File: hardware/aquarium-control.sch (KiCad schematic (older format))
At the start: 27 parts, among them M1 CONN_1, M2 CONN_1, P1 Raspberry Pi, P2 Day, P3 Night, P4 Power, P5 Switch, U1 SN74HC04, U2 MDC3105D, U3 IM06GR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

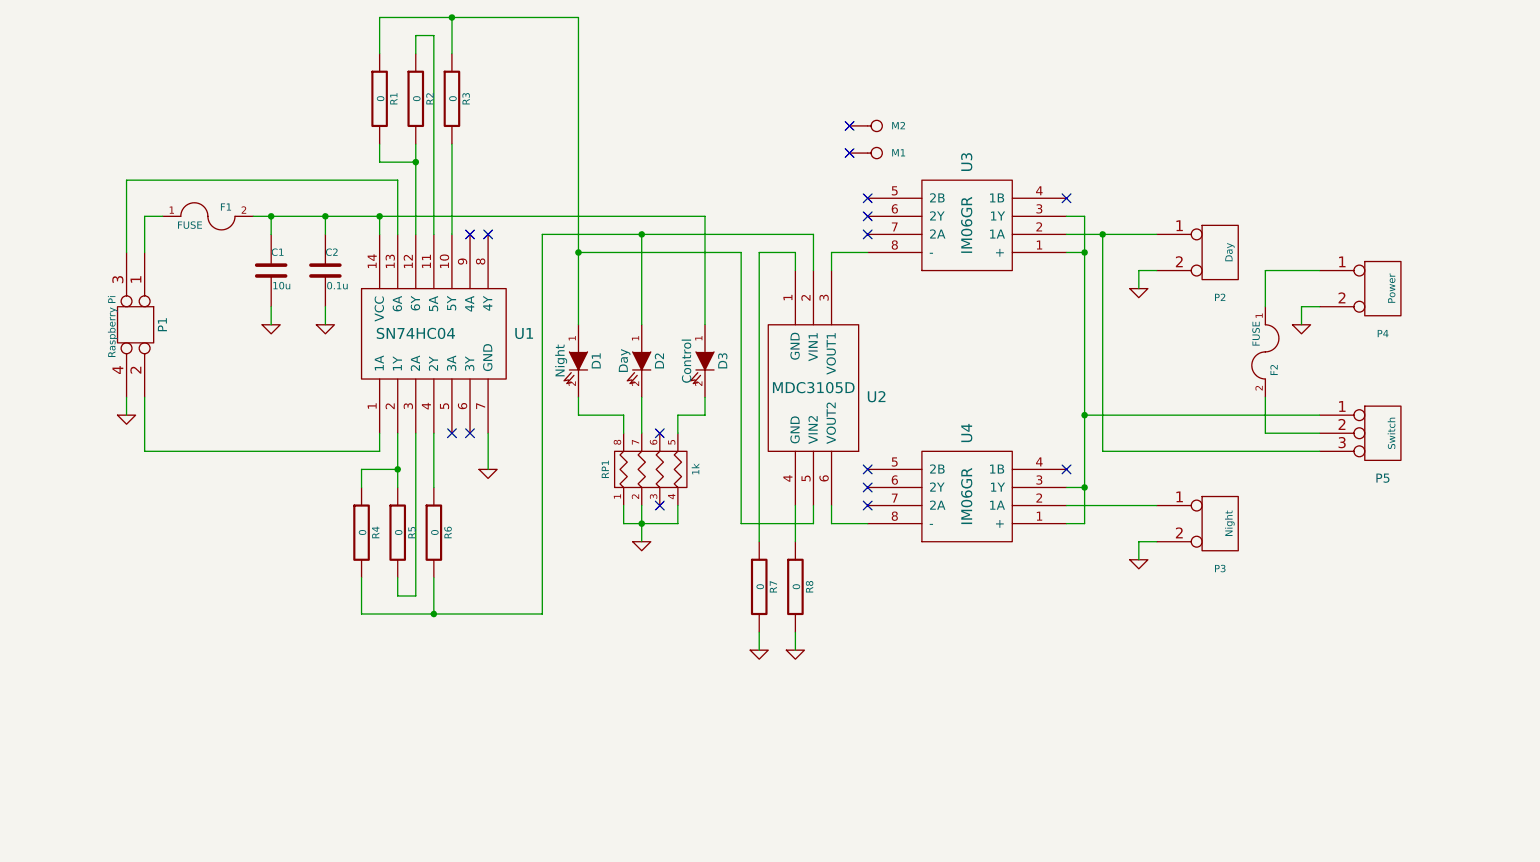
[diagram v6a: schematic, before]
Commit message: First draft of the v2 board
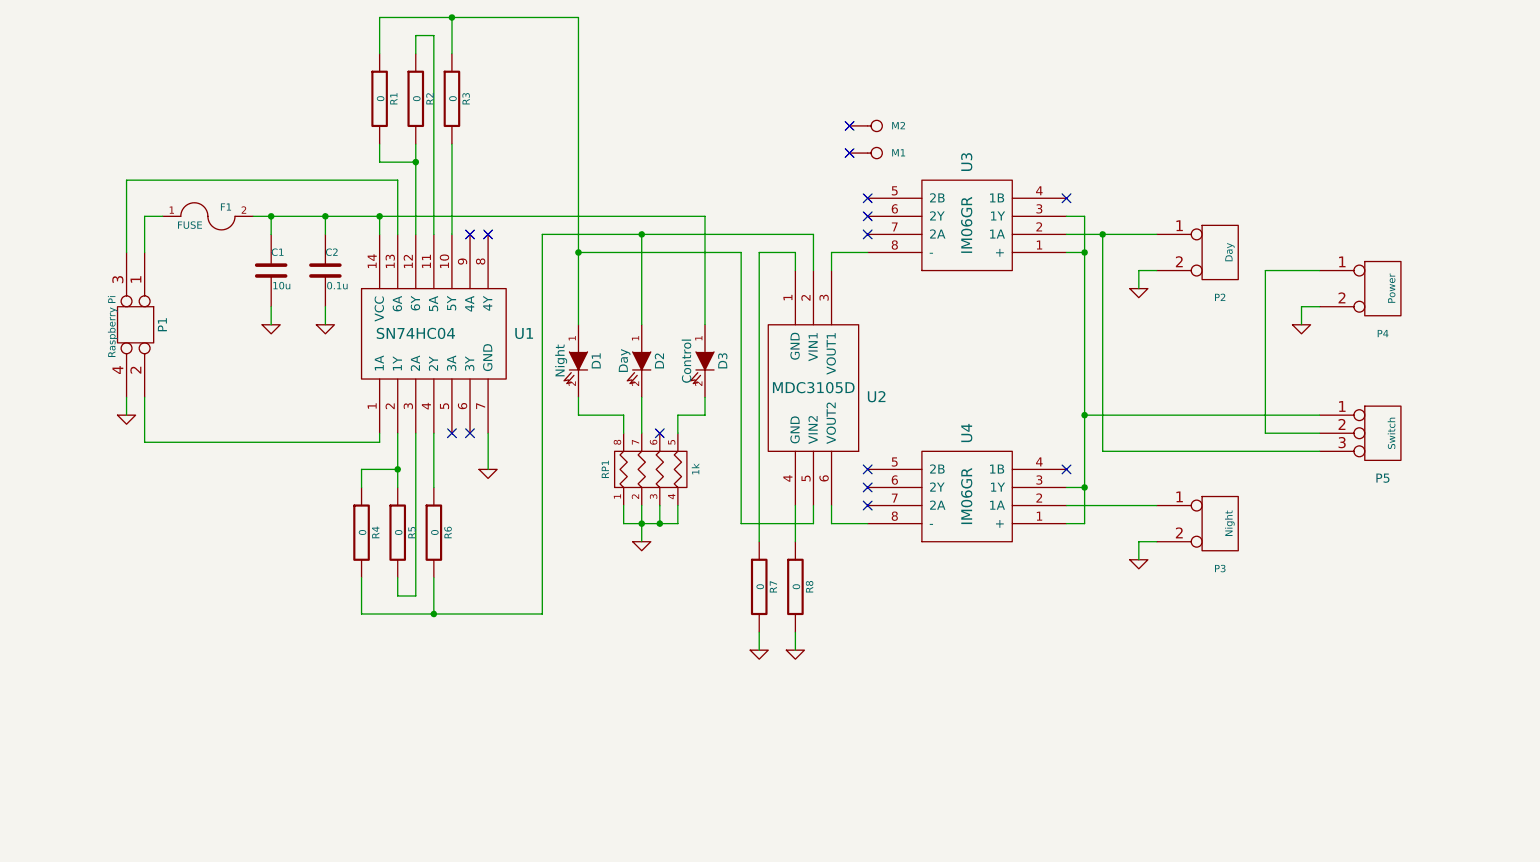
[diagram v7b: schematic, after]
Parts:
- removed F2: FUSE, symbol FUSE
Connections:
- net GND: now also RP1.3 (P3)
- net at P4.1 (P1): now also P5.2 (PM)
- no-connect marks 16 -> 15
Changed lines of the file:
@@
-EESchema Schematic File Version 2  date Sat 08 Jun 2013 07:04:43 PM PDT
+EESchema Schematic File Version 2  date 6/8/2013 9:46:08 PM
 LIBS:power
 LIBS:device
@@
 LIBS:aquarium-control-cache
 LIBS:aquarium-control-cache
-EELAYER 24 0
+EELAYER 27 0
 EELAYER END
 $Descr A4 11693 8268
@@
 Sheet 1 1
 Title ""
-Date "8 jun 2013"
+Date "9 jun 2013"
 Rev ""
 Comp ""
@@
 	1    9650 3000
 	1    0    0    -1
-$EndComp
-$Comp
-L FUSE F2
-U 1 1 5189C531
-P 9000 2550
-F 0 "F2" H 9100 2600 40  0000 C CNN
-F 1 "FUSE" H 8900 2500 40  0000 C CNN
-F 2 "" H 9000 2550 60  0001 C CNN
-F 3 "" H 9000 2550 60  0001 C CNN
-	1    9000 2550
-	0    1    1    0
 $EndComp
 $Comp
@@
 NoConn ~ 6700 1450
 NoConn ~ 6700 1300
-NoConn ~ 5650 3400
 NoConn ~ 5650 3000
 $Comp
@@
 	9200 2300 9300 2300
 Wire Wire Line
-	9300 3000 9000 3000
-Wire Wire Line
-	9000 3000 9000 2800
+	9000 3000 9300 3000
+Wire Wire Line
+	9000 2100 9000 3000
 Wire Wire Line
 	9300 2100 9000 2100
-Wire Wire Line
-	9000 2100 9000 2300
 Wire Wire Line
 	5450 3500 5450 3400
@@
 	5900 1800 5900 2400
 Connection ~ 4100 1800
-Wire Wire Line
-	2800 2800 2800 3100
-Wire Wire Line
-	2800 3100 4100 3100
-Wire Wire Line
-	4100 3100 4100 3000
 Wire Wire Line
 	2700 2000 2700 1600
@@
 Wire Wire Line
 	3500 2300 3500 2400
+Wire Wire Line
+	5650 3400 5650 3500
+Connection ~ 5650 3500
+Wire Wire Line
+	4100 3000 4100 3050
+Wire Wire Line
+	4100 3050 2800 3050
+Wire Wire Line
+	2800 3050 2800 2800
 $EndSCHEMATC

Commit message: Updated the schematic to use a 5v rail for the relays
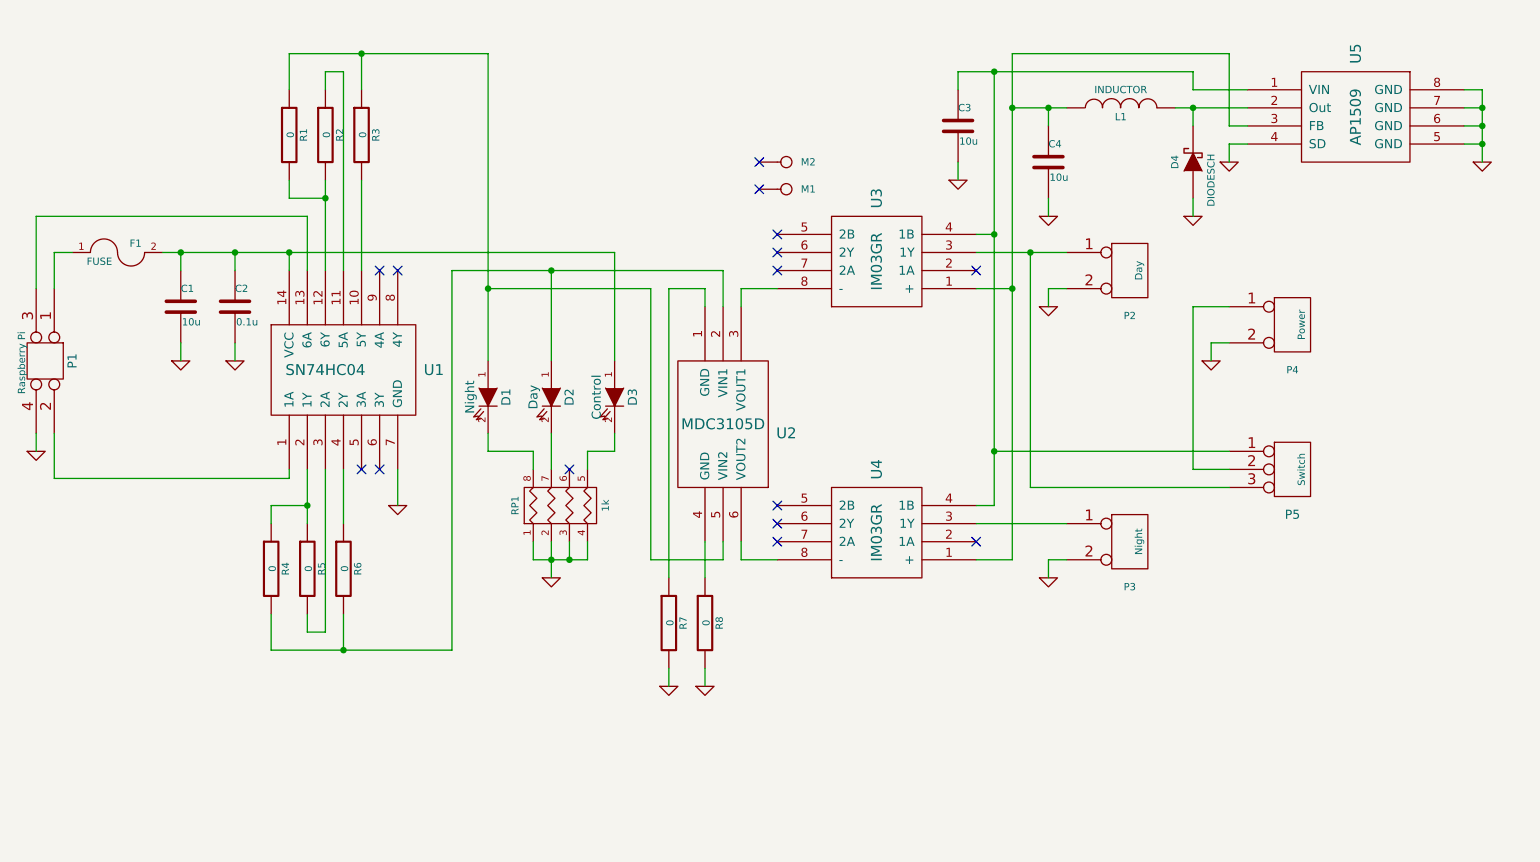
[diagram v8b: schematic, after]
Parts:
- added C3, C4: 10u, ~, symbol C
- added D4: DIODESCH, ~, symbol DIODESCH
- added L1: INDUCTOR, ~, symbol INDUCTOR
- added U5: AP1509, ~, symbol AP1509
- U3, U4: value IM06GR -> IM03GR
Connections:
- net GND: now also C3.2, C4.2, D4.1 (A), U5.4 (SD), U5.5 (GND), U5.6 (GND), U5.7 (GND), U5.8 (GND)
- net at P2.1 (P1), P5.3 (P3): now also U3.3 (1Y); no longer U3.2 (1A)
- net at P3.1 (P1): now also U4.3 (1Y); no longer U4.2 (1A)
- net at U3.4 (1B): now also P5.1 (P1), U4.4 (1B), C3.1, U5.1 (VIN)
- new net: C4.1, L1.1, U3.1 (+), U4.1 (+), U5.3 (FB)
- new net: D4.2 (K), L1.2, U5.2 (Out)
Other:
- moved on the sheet: C1, C2, D1, D2, D3, F1, M1, M2, P1, P2, P3, P4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
